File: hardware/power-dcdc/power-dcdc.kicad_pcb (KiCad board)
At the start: 2 copper layers, 110 x 70 mm, 67 parts, among them J1 SOLAR_IN, J2 BATT2, J3 BATT1, J4 DCDC-MEASURES, J5 DCDC-PWM, Q1 SIR164ADP, Q2 SIR164ADP, Q3 SI7149ADP, Q4 SI7149ADP, Q5 SI7149ADP, Q6 SI7149ADP, U1 LP4951C, U2 NCP5901B, U3 PAC1953-1, U4 DGD0215, U5 DGD0215

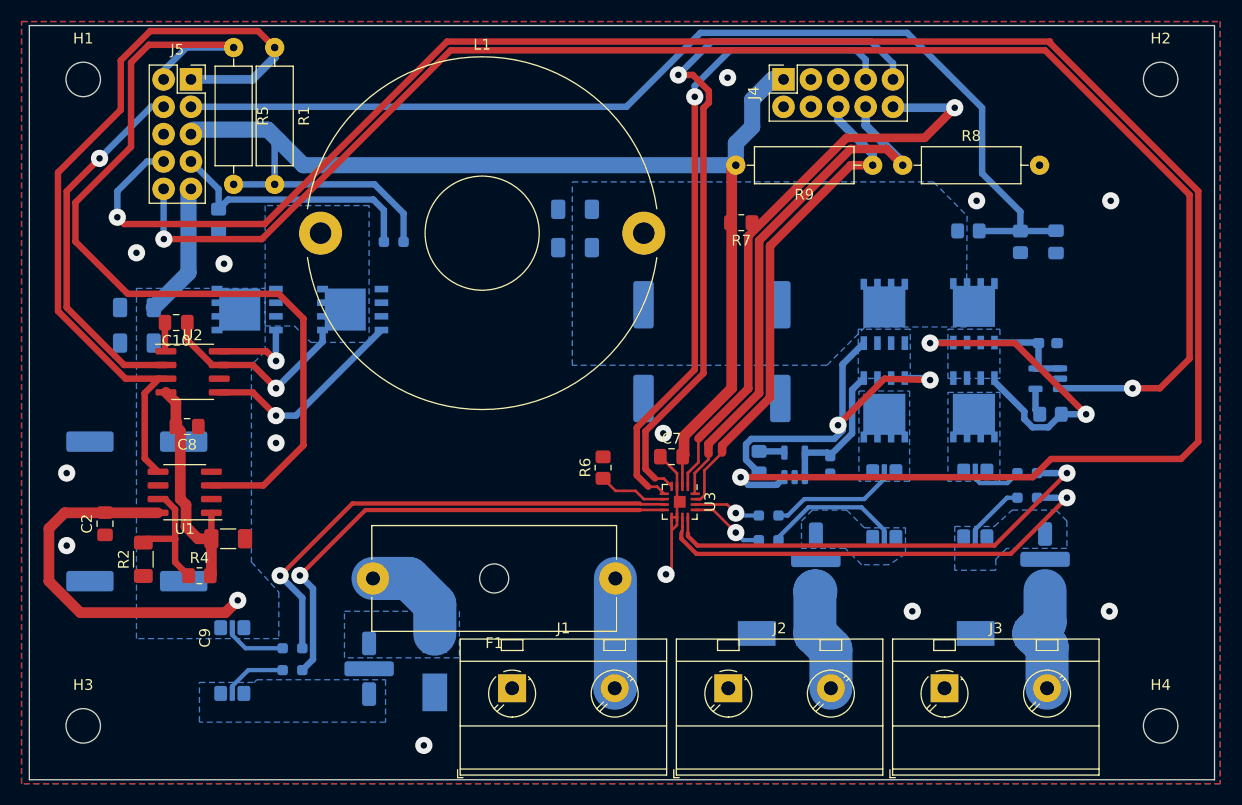
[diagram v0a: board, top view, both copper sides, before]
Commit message: Adjust PCBs after reference and footprint changes
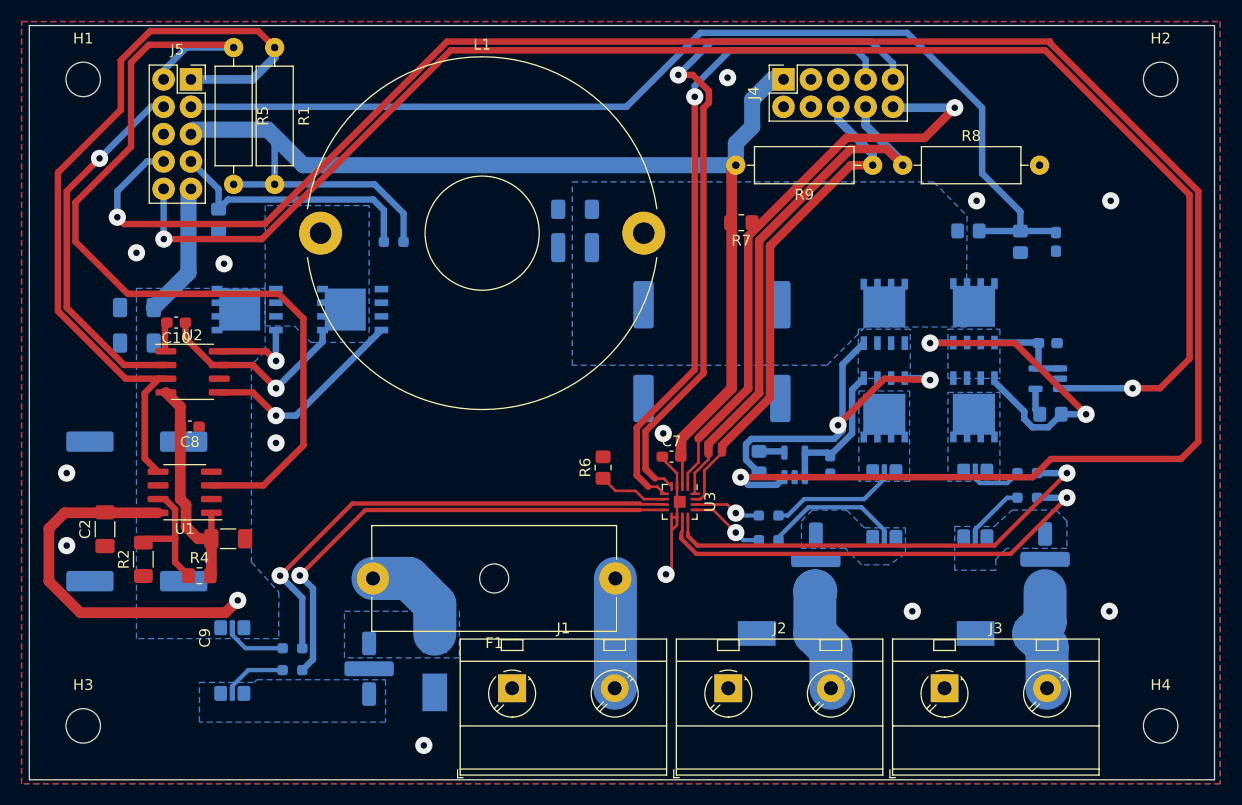
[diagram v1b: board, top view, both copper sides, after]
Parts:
- C10, C19, C7, C8: footprint Capacitor_SMD:C_0805_2012Metric_Pad1.18x1.45mm_HandSolder -> Capacitor_SMD:C_0603_1608Metric_Pad1.08x0.95mm_HandSolder
- C12: footprint Capacitor_SMD:C_1206_3216Metric_Pad1.33x1.80mm_HandSolder -> Capacitor_SMD:C_1210_3225Metric_Pad1.33x2.70mm_HandSolder
- C2: footprint Capacitor_SMD:C_0805_2012Metric_Pad1.18x1.45mm_HandSolder -> Capacitor_SMD:C_1206_3216Metric_Pad1.33x1.80mm_HandSolder
- Q3, Q4, Q5, Q6: value SI7149ADP -> SI7149ADP
- moved C2 0.51 mm to (57.0, 126.7)
- moved C8 0.25 mm to (64.9, 117.2)

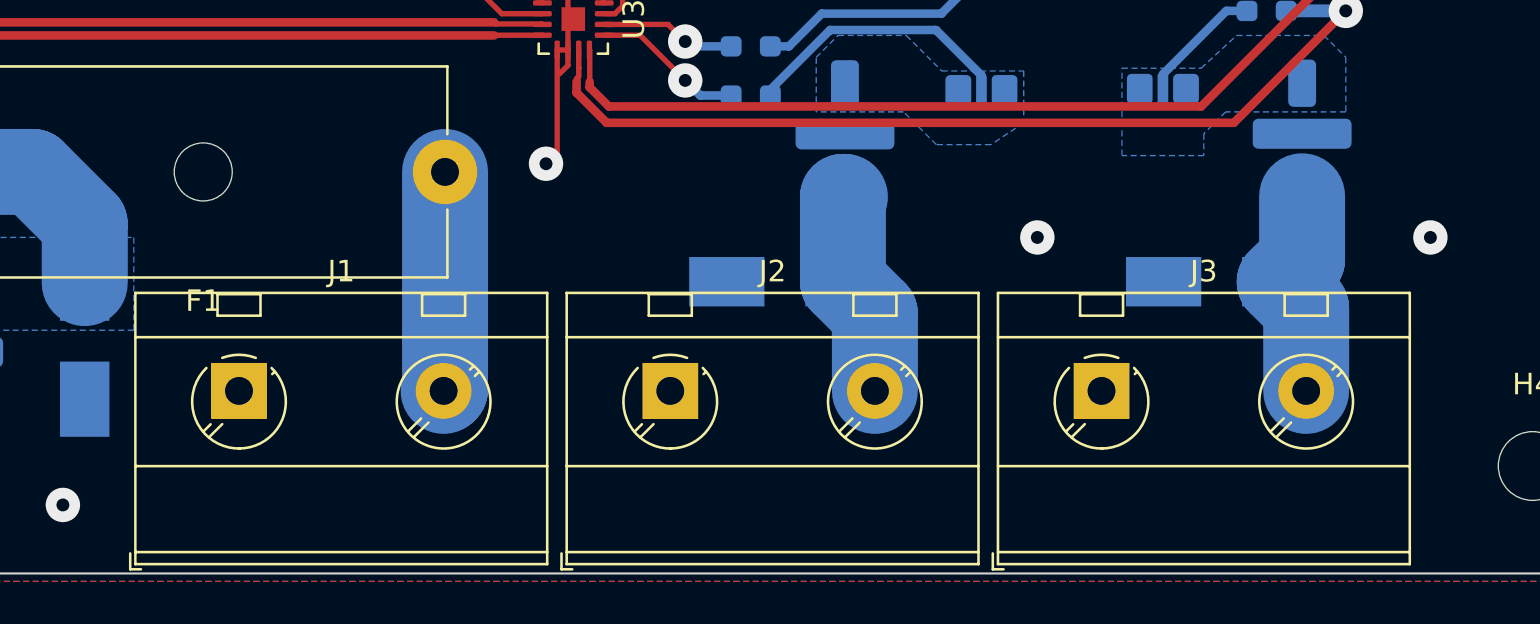
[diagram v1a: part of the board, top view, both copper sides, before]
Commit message: power-dcdc: move power connectors closer to edge, the connectors used are actually a bit smaller than footprint
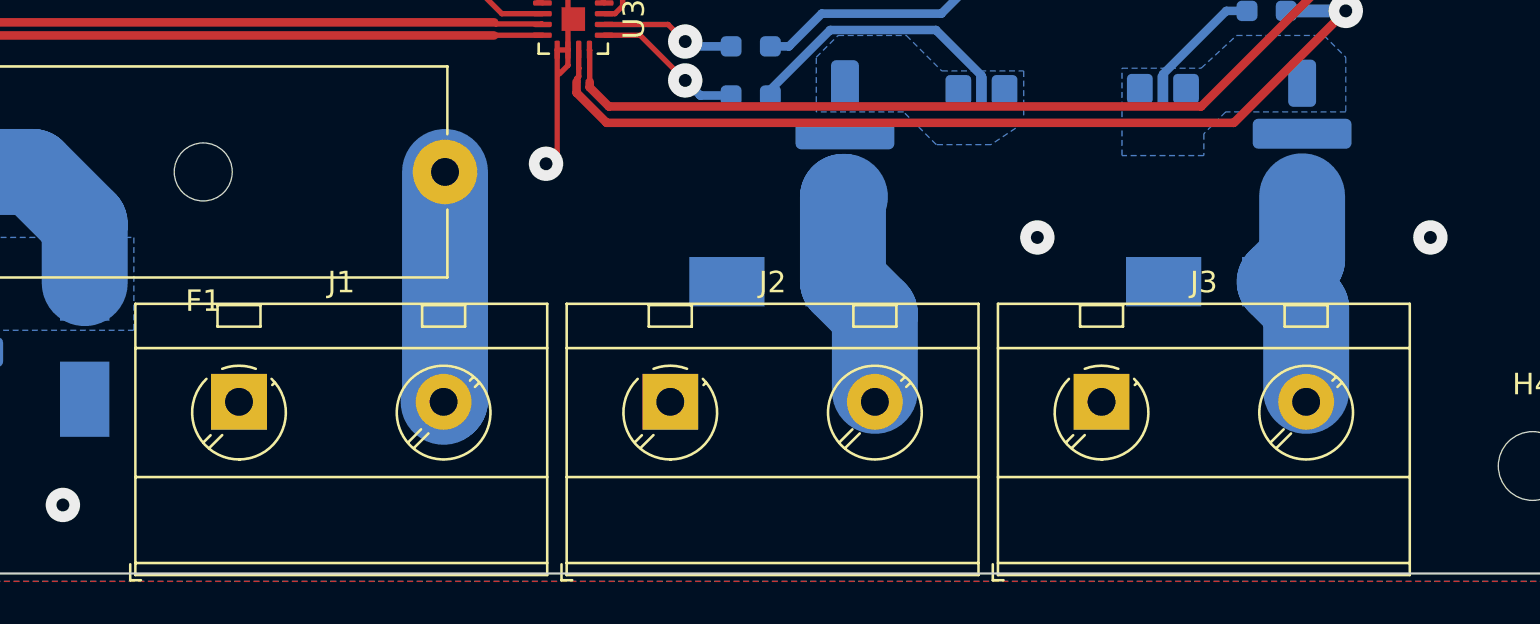
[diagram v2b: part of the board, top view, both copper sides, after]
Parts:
- moved J1 0.51 mm to (94.8, 142.0)
- moved J2 0.51 mm to (114.9, 142.0)
- moved J3 0.51 mm to (134.9, 142.0)
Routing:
- net Net-(F1-Pad1): track 10.2 -> 10.7 mm
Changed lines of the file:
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@@
   )
   (footprint "TerminalBlock_MetzConnect:TerminalBlock_MetzConnect_Type703_RT10N02HGLU_1x02_P9.52mm_Horizontal" locked (layer "F.Cu")
-    (at 114.874 141.506)
+    (at 114.874 142.014)
     (descr "terminal block Metz Connect Type703_RT10N02HGLU, 2 pins, pitch 9.52mm, size 19x12.5mm^2, drill diamater 1.3mm, pad diameter 2.6mm, see http://www.metz-connect.com/de/system/files/productfiles/Datenblatt_317031_RT10NxxHGLU_OFF-022897S.pdf, script-generated using https://github.com/pointhi/kicad-footprint-generator/scripts/TerminalBlock_MetzConnect")
     (tags "THT terminal block Metz Connect Type703_RT10N02HGLU pitch 9.52mm size 19x12.5mm^2 drill 1.3mm pad 2.6mm")
@@
   )
   (footprint "TerminalBlock_MetzConnect:TerminalBlock_MetzConnect_Type703_RT10N02HGLU_1x02_P9.52mm_Horizontal" locked (layer "F.Cu")
-    (at 134.94 141.506)
+    (at 134.94 142.014)
     (descr "terminal block Metz Connect Type703_RT10N02HGLU, 2 pins, pitch 9.52mm, size 19x12.5mm^2, drill diamater 1.3mm, pad diameter 2.6mm, see http://www.metz-connect.com/de/system/files/productfiles/Datenblatt_317031_RT10NxxHGLU_OFF-022897S.pdf, script-generated using https://github.com/pointhi/kicad-footprint-generator/scripts/TerminalBlock_MetzConnect")
     (tags "THT terminal block Metz Connect Type703_RT10N02HGLU pitch 9.52mm size 19x12.5mm^2 drill 1.3mm pad 2.6mm")
@@
   )
   (footprint "TerminalBlock_MetzConnect:TerminalBlock_MetzConnect_Type703_RT10N02HGLU_1x02_P9.52mm_Horizontal" locked (layer "F.Cu")
-    (at 94.808 141.506)
+    (at 94.808 142.014)
     (descr "terminal block Metz Connect Type703_RT10N02HGLU, 2 pins, pitch 9.52mm, size 19x12.5mm^2, drill diamater 1.3mm, pad diameter 2.6mm, see http://www.metz-connect.com/de/system/files/productfiles/Datenblatt_317031_RT10NxxHGLU_OFF-022897S.pdf, script-generated using https://github.com/pointhi/kicad-footprint-generator/scripts/TerminalBlock_MetzConnect")
     (tags "THT terminal block Metz Connect Type703_RT10N02HGLU pitch 9.52mm size 19x12.5mm^2 drill 1.3mm pad 2.6mm")
@@
   (segment (start 143.6635 111.551) (end 143.3885 111.826) (width 0.6) (layer "B.Cu") (net 13))
   (segment (start 139.573 109.422) (end 143.6115 109.422) (width 0.6) (layer "B.Cu") (net 13))
-  (segment (start 104.394 141.44) (end 104.328 141.506) (width 4) (layer "B.Cu") (net 14))
-  (segment (start 104.394 131.318) (end 104.394 141.44) (width 4) (layer "B.Cu") (net 14))
+  (segment (start 104.394 131.318) (end 104.394 141.948) (width 4) (layer "B.Cu") (net 14))
+  (segment (start 104.394 141.948) (end 104.328 142.014) (width 4) (layer "B.Cu") (net 14))
   (segment (start 73.279 131.064) (end 79.985 124.358) (width 0.4) (layer "F.Cu") (net 16))
   (segment (start 79.985 124.358) (end 106.68 124.358) (width 0.4) (layer "F.Cu") (net 16))

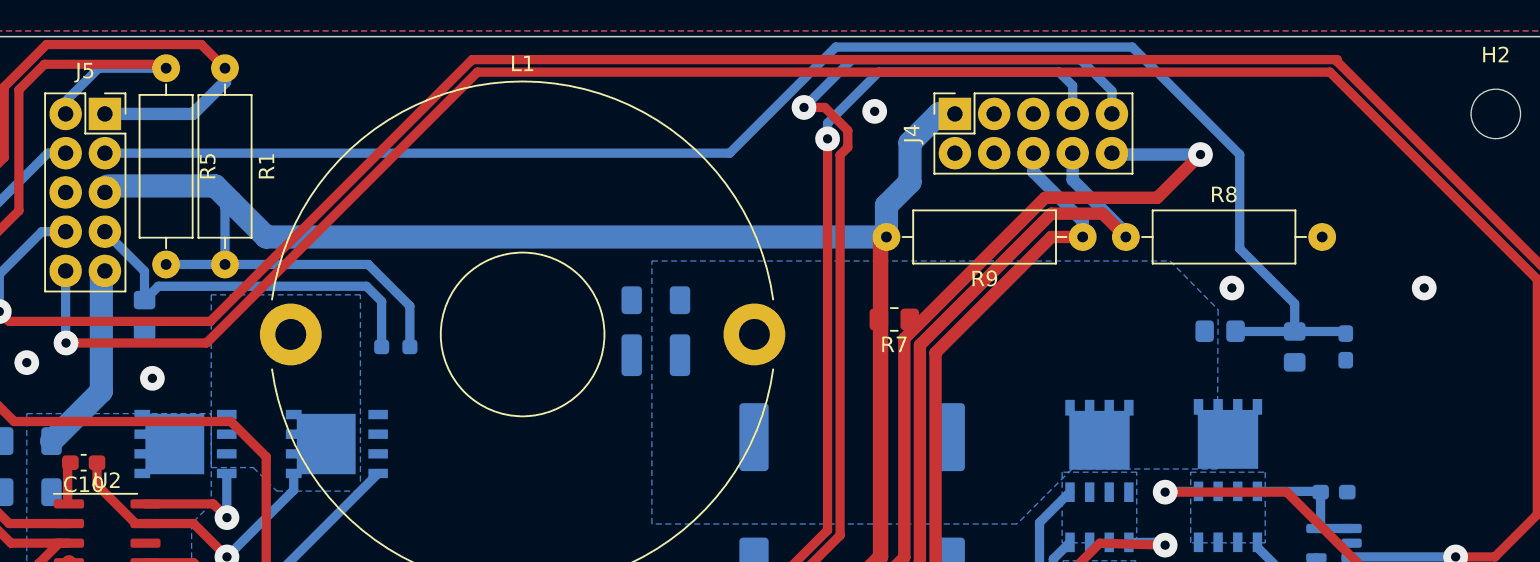
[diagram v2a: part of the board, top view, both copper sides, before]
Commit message: On second though, the pac1953  won't be fast enough for the PWM regulation loop. So add a resistor divider routed to RA5 to get the solar voltage from the PIC18's ADC.
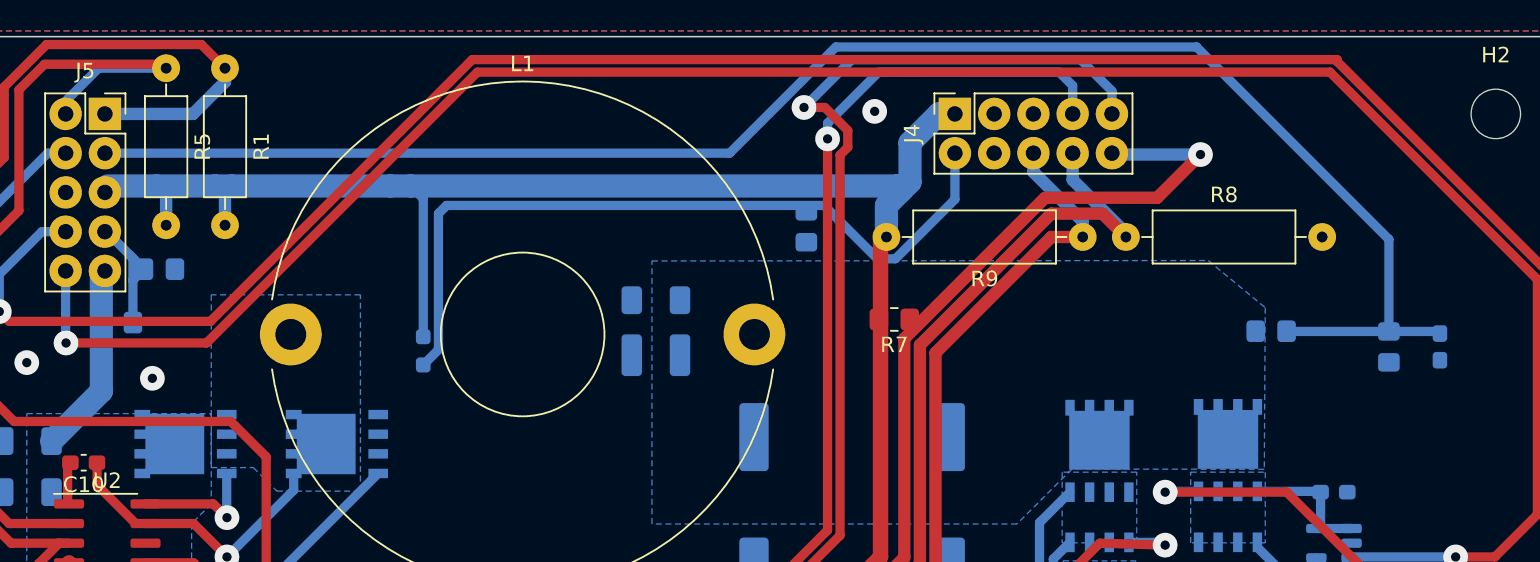
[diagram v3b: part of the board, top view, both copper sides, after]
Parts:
- added R17: 22k, Resistor_SMD:R_0805_2012Metric_Pad1.20x1.40mm_HandSolder, B.Cu at (65.8, 98.5)
- added R18: 1.74k, Resistor_SMD:R_0805_2012Metric_Pad1.20x1.40mm_HandSolder, B.Cu at (68.5, 95.0)
- R1, R5: footprint Resistor_THT:R_Axial_DIN0309_L9.0mm_D3.2mm_P12.70mm_Horizontal -> Resistor_THT:R_Axial_DIN0207_L6.3mm_D2.5mm_P10.16mm_Horizontal
- moved R16 43.2 mm to (110.4, 92.3)
- moved R15 6.10 mm to (148.1, 100.1)
- moved C19 6.10 mm to (151.4, 100.1)
- moved R14 3.30 mm to (140.5, 99.1)
- moved TH1 1.80 mm to (85.6, 100.3), turned to -90 degrees
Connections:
- J4 pad 2: unconnected-(J4-Pad2) -> /TH
- J5 pad 7: /TH -> /Solar_V
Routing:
- net /TH: track 24.5 -> 49.8 mm
- net /Solar_V: track 0.00 -> 8.87 mm
- net +5V: track 117.6 -> 109.2 mm
- net PWM_V: track 99.1 -> 106.9 mm
- net GND: vias 13 -> 11

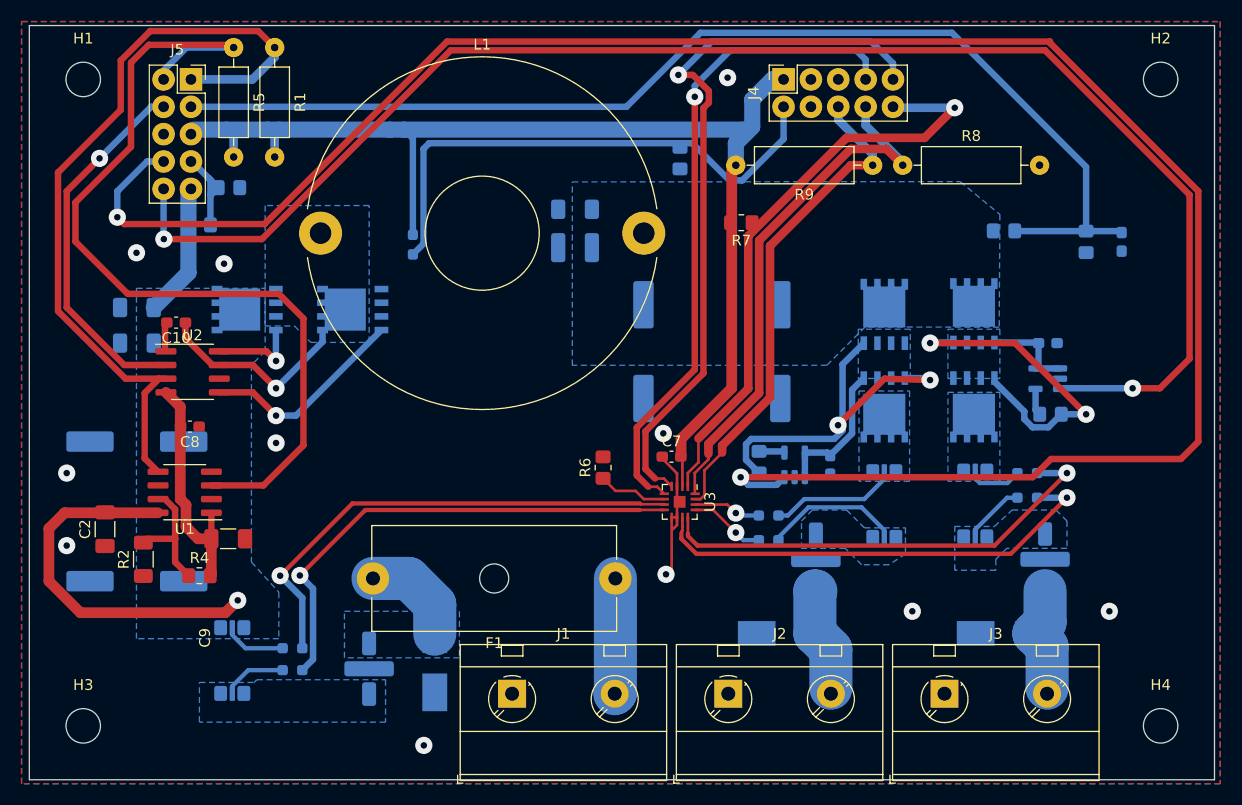
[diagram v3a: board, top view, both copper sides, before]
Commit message: Re-annotate schematics
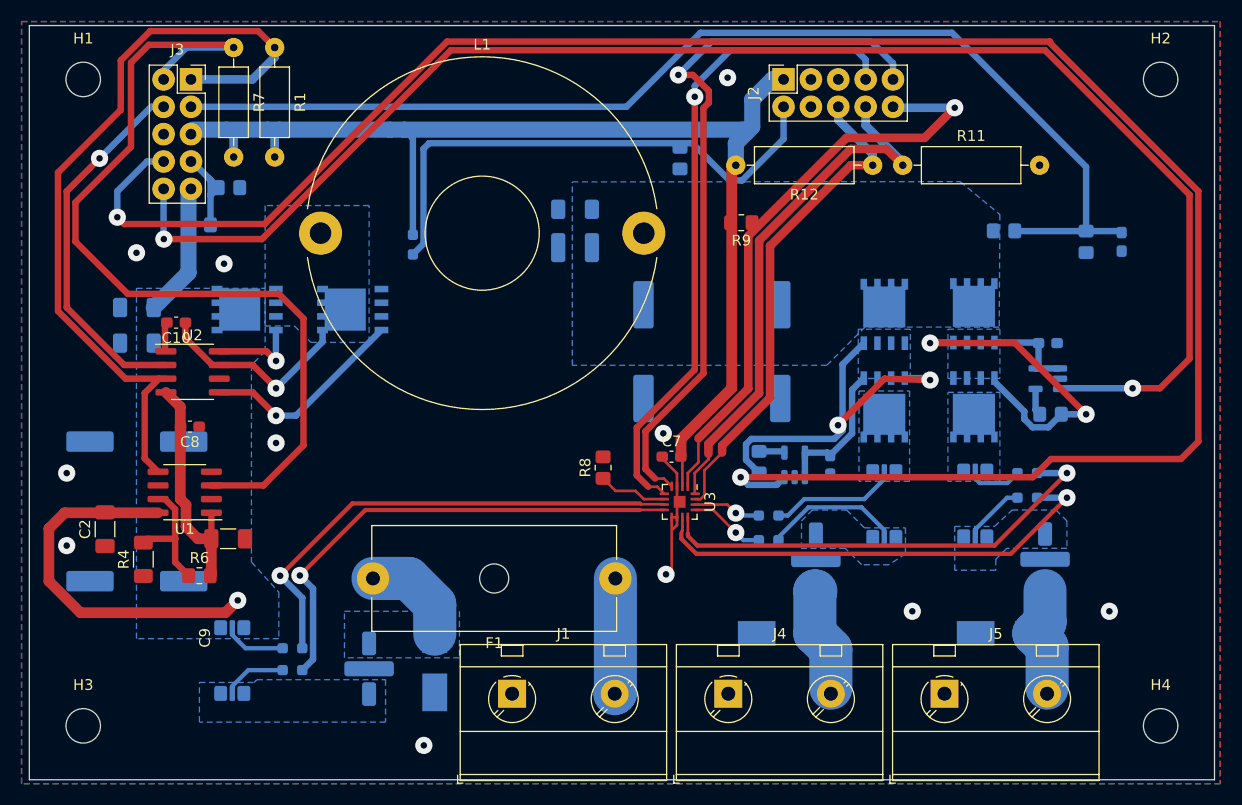
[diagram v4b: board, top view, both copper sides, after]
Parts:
- renumbered J4 to J2, J5 to J3, J2 to J4, J3 to J5, R16 to R10, R8 to R11, R9 to R12, R10 to R13, R11 to R14, R12 to R15, R13 to R16, R14 to R17, R15 to R18, R17 to R2, R18 to R3, R2 to R4, R3 to R5, R4 to R6, R5 to R7, R6 to R8, R7 to R9
